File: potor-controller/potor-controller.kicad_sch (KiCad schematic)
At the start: 8 parts, among them U1 STM32G474CEUx

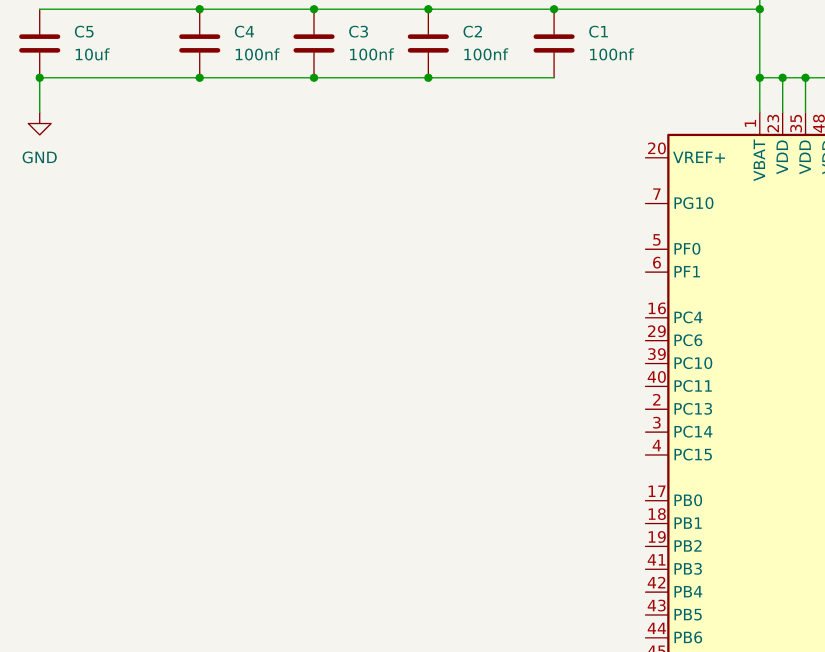
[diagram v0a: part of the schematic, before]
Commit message: add RH100-8 crystal
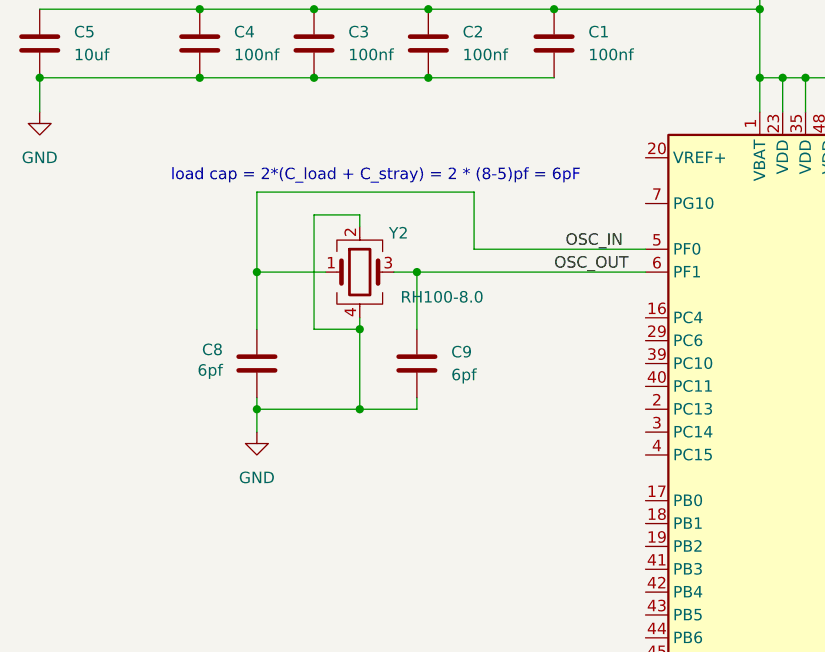
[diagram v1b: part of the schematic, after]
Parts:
- added C8, C9: 6pf, symbol Device:C
- added Y2: RH100-8.0, symbol Device:Crystal_GND24
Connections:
- net +3V3A: now also C8.1, C9.2, Y2.2, Y2.4
- net OSC_IN: now reaches U1.5 (PF0)
- net OSC_IN: now also C8.2, Y2.1
- net OSC_OUT: now reaches U1.6 (PF1)
- net OSC_OUT: now also C9.1, Y2.3
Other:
- note added: "load cap = 2*(C_load + C_stray) = 2 * (8-5)pf = 6pF"

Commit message: add SWD, NRST pins
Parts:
- added J1: Conn_01x05_Pin, symbol Connector:Conn_01x05_Pin
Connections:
- net +3V3: now also J1.1 (Pin_1)
- net +3V3A: now also J1.2 (Pin_2)
- net at U1.36 (PA13): now also J1.4 (Pin_4)
- net at U1.37 (PA14): now also J1.5 (Pin_5)
- net NRST: now reaches U1.7 (PG10)
- net NRST: now also J1.3 (Pin_3)

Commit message: add 3v3 linear regulator
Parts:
- added C10: 100nf, symbol Device:C
- added C11: 1uf, symbol Device:C
- added C12, C13: 10uF, symbol Device:C
- added D1: LED, symbol Device:LED
- added FB1: 120R @ 100MHz, Inductor_SMD:L_0603_1608Metric, symbol Device:FerriteBead
- added R1: 1k5, symbol Device:R
- added U2: DRV8323, Package_DFN_QFN:Texas_RHA0040E_VQFN-40-1EP_6x6mm_P0.5mm_EP3.52x2.62mm, symbol Driver_Motor:DRV8308
- added U3: REG1117-3.3, symbol Regulator_Linear:AZ1117-3.3
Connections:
- net +3V3: now also C11.1, C13.1, D1.2 (A), FB1.2, U3.2 (VO)
- net +3V3A: now also C10.1, C11.2, C12.2, C13.2, FB1.1, R1.2, U3.1 (GND)
- net NRST: now also C10.2
- net SWDIO: now reaches J1.4 (Pin_4), U1.36 (PA13)
- net SWCLK: now reaches J1.5 (Pin_5), U1.37 (PA14)
- new net +12V: C12.1, U3.3 (VI)
- new net led_cat: D1.1 (K), R1.1
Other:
- note added: "10uF tantalum. >=50uF electrolytic"
- note removed: "add ferrite bead to 3v3 digital?"
- moved on the sheet: C1, C2, C3, C4, C5, C6, C7, C8, C9, J1, U1, Y2

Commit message: correct drv8323 symbol, choose fet
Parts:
- added Q1: SiR182DP, Package_SO:PowerPAK_SO-8_Single, symbol Transistor_FET:SiR696DP
- added R2: 100, symbol Device:R
- added U4: DRV8323HRTAR, RTA0040B, symbol 2024-03-31_18-49-26:DRV8323HRTAR
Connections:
- new net: Q1.4 (G), R2.2
- new net: Q1.1 (S), Q1.2 (S), Q1.3 (S)
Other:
- note added: "gate resistors limit current, <= 0603, ~100ohm"

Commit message: add sense, adjust drv symbol, add notation
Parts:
- removed U2: DRV8323, Package_DFN_QFN:Texas_RHA0040E_VQFN-40-1EP_6x6mm_P0.5mm_EP3.52x2.62mm, symbol Driver_Motor:DRV8308
- added C14, C15, C16: 1uf, symbol Device:C
- added C17: 47nF, symbol Device:C
- added C18, C19, C21: 1uF, symbol Device:C
- added C20: 10uf, symbol Device:C
- added C22, C23, C24: .1uf, symbol Device:C
- added Q2, Q3, Q4, Q5, Q6: SiR182DP, Package_SO:PowerPAK_SO-8_Single, symbol Transistor_FET:SiR696DP
- added R10, R4, R7: 0.001, symbol Device:R
- added R11, R12, R13: 1k5, symbol Device:R
- added R3, R5, R6, R8, R9: 100, symbol Device:R
- added U2, U5, U6: INA240A2D, Package_SO:SOIC-8_3.9x4.9mm_P1.27mm, symbol Amplifier_Current:INA240A2D
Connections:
- net +12V: now also Q1.5 (D), C14.1, C15.1, C16.1, Q3.5 (D), Q5.5 (D); no longer C12.1, U3.3 (VI)
- net +3V3: now also U4.4 (VM), C18.1, C19.1, C20.1, C22.1, C23.1, C24.1, R11.1, R12.1, U2.6 (V+), U5.6 (V+), U6.6 (V+)
- net +3V3A: now also U4.29 (GAIN_SCS_N), U4.32 (AGND), U4.40 (PGND), U4.41 (PAD), C14.2, C15.2, C16.2, C19.2, C20.2, C21.2, C22.2, C23.2, C24.2, Q2.1 (S), Q2.2 (S), Q2.3 (S), Q4.1 (S), Q4.2 (S), Q4.3 (S), Q6.1 (S), Q6.2 (S), Q6.3 (S), R13.2, U2.2 (GND), U2.4 (GND), U5.2 (GND), U5.4 (GND), U6.2 (GND), U6.4 (GND)
- net w_sense: now reaches U1.10 (PA2)
- net w_sense: now also U6.5
- net pwm_Vn: now reaches U1.17 (PB0)
- net pwm_Vn: now also U4.37 (INLB)
- net pwm_Wn: now reaches U1.18 (PB1)
- net pwm_Wn: now also U4.39 (INLC)
- net pwm_Un: now reaches U1.2 (PC13)
- net pwm_Un: now also U4.35 (INLA)
- net pwm_U: now reaches U1.30 (PA8)
- net pwm_U: now also U4.34 (INHA)
- net pwm_V: now reaches U1.31 (PA9)
- net pwm_V: now also U4.36 (INHB)
- net pwm_W: now reaches U1.32 (PA10)
- net pwm_W: now also U4.38 (INHC)
- net u_sense: now reaches U1.8 (PA0)
- net u_sense: now also U5.5
- net v_sense: now reaches U1.9 (PA1)
- net v_sense: now also U2.5
- net at U4.1 (CPL): now also C17.2
- net at U4.13 (GLB): now also R6.2
- net v sense 1: now reaches U4.14 (SHB)
- net v sense 1: now also Q3.1 (S), Q3.2 (S), Q3.3 (S), Q4.5 (D), R7.1, U2.8 (+)
- net at U4.15 (GHB): now also R5.1
- net at U4.16 (GHC): now also R8.1
- net w sense 1: now reaches U4.17 (SHC)
- net w sense 1: now also Q5.1 (S), Q5.2 (S), Q5.3 (S), Q6.5 (D), R10.1, U6.8 (+)
- net at U4.18 (GLC): now also R9.2
- net at U4.2 (CPH): now also C17.1
- net sdo: now reaches U4.26 (MODE_SDO)
- net sdo: now also R11.2
- net sdi: now reaches U4.27 (IDRIVE_SDI)
- net sclk: now reaches U4.28 (VDS_SCLK)
- net at U4.3 (VCP): now also C18.2
- net at U4.33 (DVDD): now also C21.1
- net at U4.6 (GHA): now also R2.1
- net u sense 1: now reaches U4.7 (SHA)
- net u sense 1: now also Q1.1 (S), Q1.2 (S), Q1.3 (S), Q2.5 (D), R4.1, U5.8 (+)
- net at U4.8 (GLA): now also R3.2
- new net: Q5.4 (G), R8.2
- new net: R12.2, R13.1, U2.3 (REF2), U2.7 (REF1), U5.3 (REF2), U5.7 (REF1), U6.3 (REF2), U6.7 (REF1)
- new net: Q6.4 (G), R9.1
- new net: Q3.4 (G), R5.2
- new net: Q2.4 (G), R3.1
- new net: Q4.4 (G), R6.1
- new net VCC +12V: C12.1, U3.3 (VI)
- new net u: R4.2, U5.1 (-)
- new net v: R7.2, U2.1 (-)
- new net w: R10.2, U6.1 (-)
- no-connect marks 0 -> 12
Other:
- note added: ""connecting both pins together and then to a reference voltage results in an output voltage equal to the reference voltage" (shorted input) voltage divider for .5(3v3) = 1.65v midpoint"
- note added: "Driver"
- note added: "POTOR CONTROLLER :)"
- note added: "Power"
- note added: "SPI for driver and sense config. I'm leaving sense alone since I'm not using low-side sensing"
- note added: "STM32"
- note added: "Sense"
- note added: "amp is INA240A2D "A2" = 50v/v gain max current ~20A? 20x0.001 = 0.02v x gain (50) = 1v + 1.65v midpoint = 2.65 checks out"
- note added: "logic low enables spi >"
- note added: "sense resistor"
- moved on the sheet: C10, J1, Q1, R2
